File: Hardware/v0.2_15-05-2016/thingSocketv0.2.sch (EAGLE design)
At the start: 32 parts

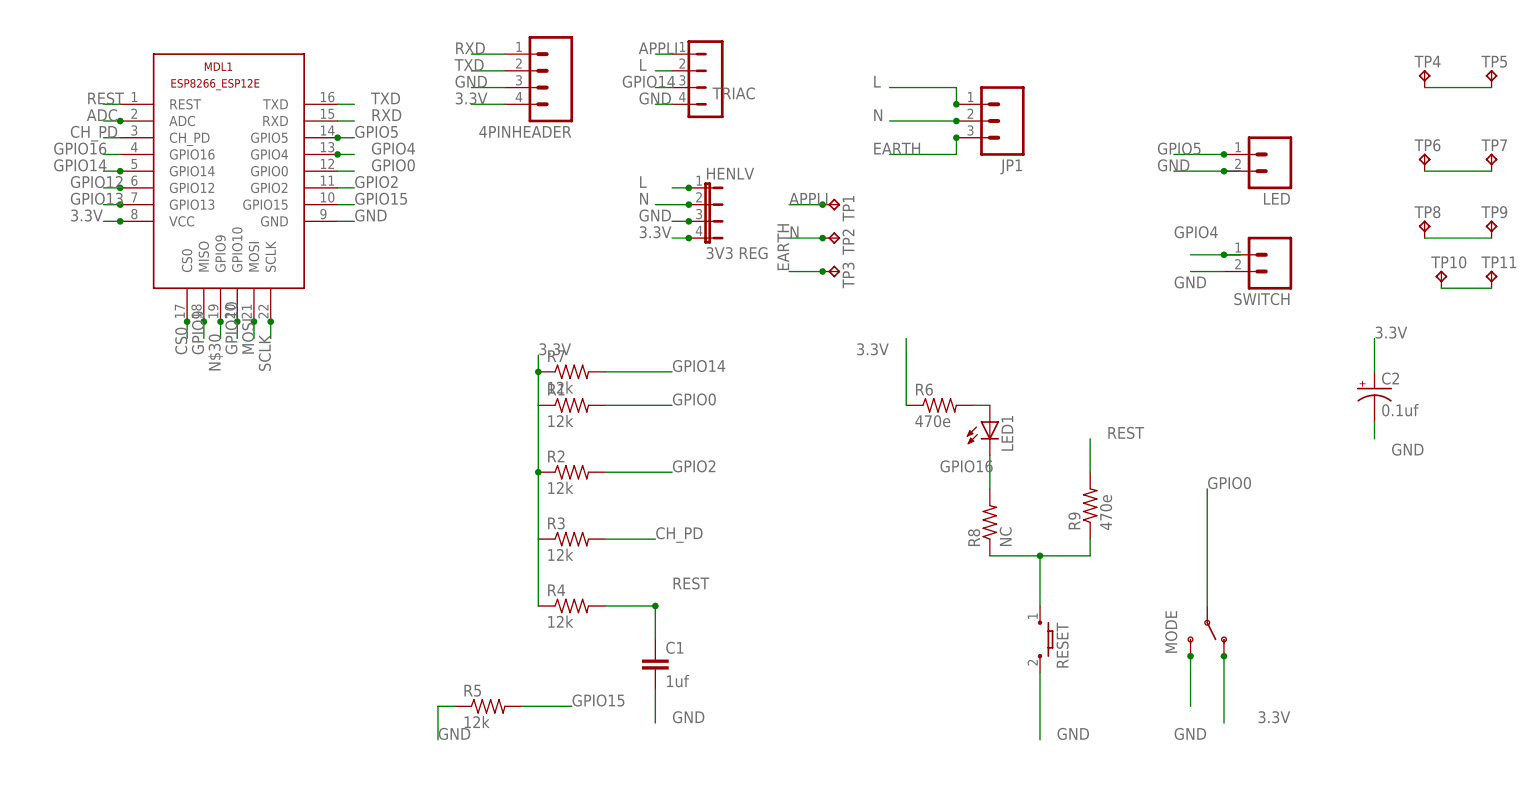
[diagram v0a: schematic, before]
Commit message: unified the resource mechanism; added device password
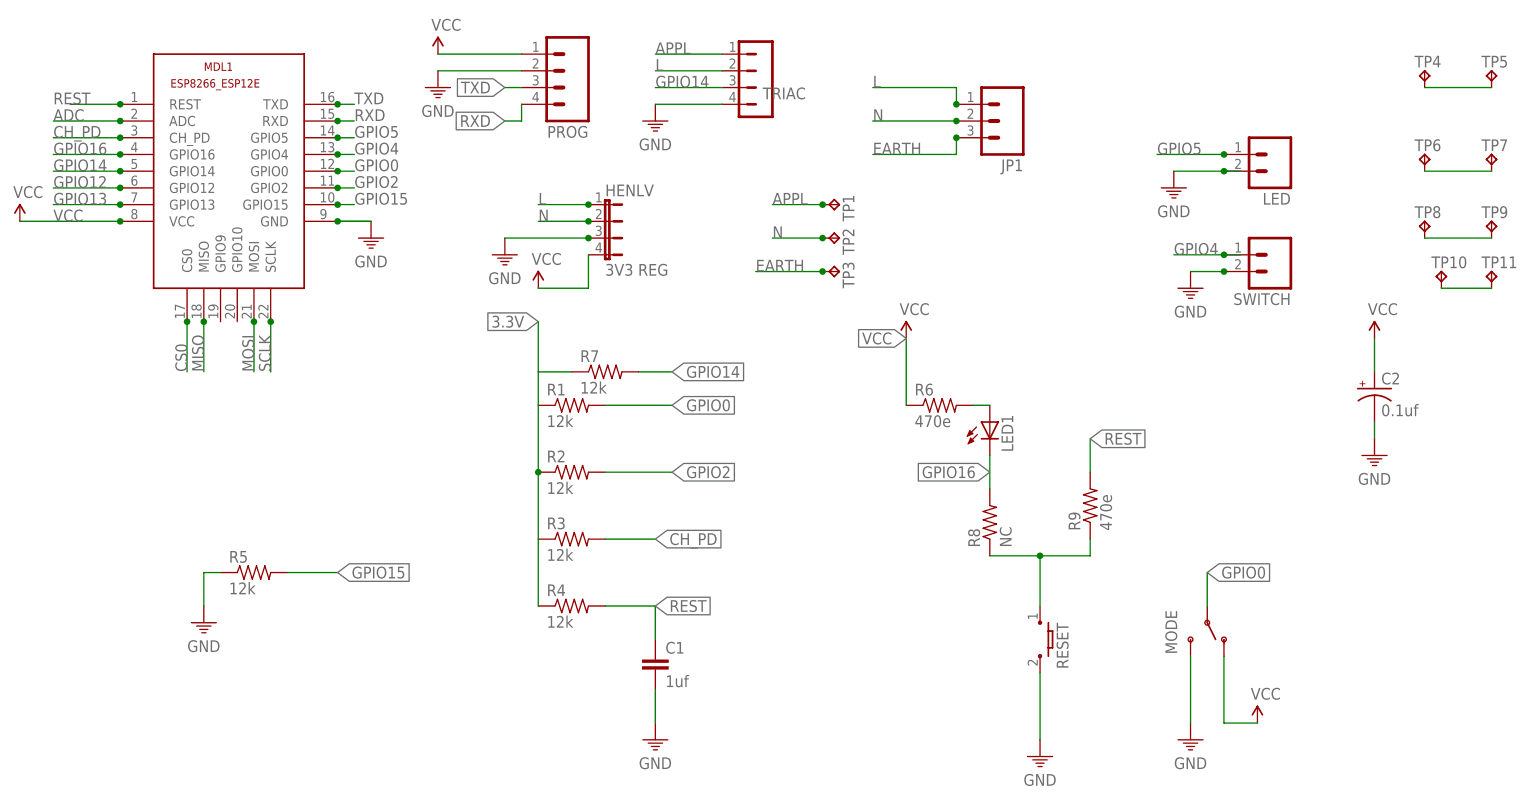
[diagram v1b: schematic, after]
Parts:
- removed 4PINHEADER: (no value), con-oupiin:M04-V
- added PROG: (no value), con-oupiin:M04-V
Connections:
- net APPLI renamed APPL
- net GPIO9 renamed MISO
- removed net GPIO10: MDL1.GPIO10
- removed net N$30: MDL1.GPIO9
- new net VCC: C2.+, HENLV.4, MDL1.VCC, MODE.O, PROG.1, R6.1
- net 3.3V: no longer 4PINHEADER.4, C2.+, HENLV.4, MDL1.VCC, MODE.O, R6.1
- net GND: no longer 4PINHEADER.3
- net RXD: now also PROG.4; no longer 4PINHEADER.1
- net TXD: now also PROG.2, PROG.3; no longer 4PINHEADER.2
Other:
- moved on the sheet: HENLV, R5, R7, TRIAC

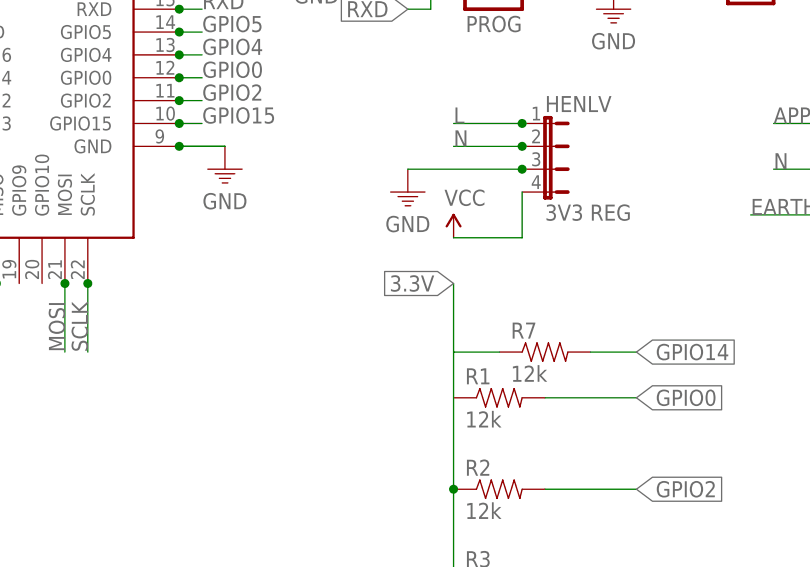
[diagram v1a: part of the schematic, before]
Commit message: added default mechanism for factory reset
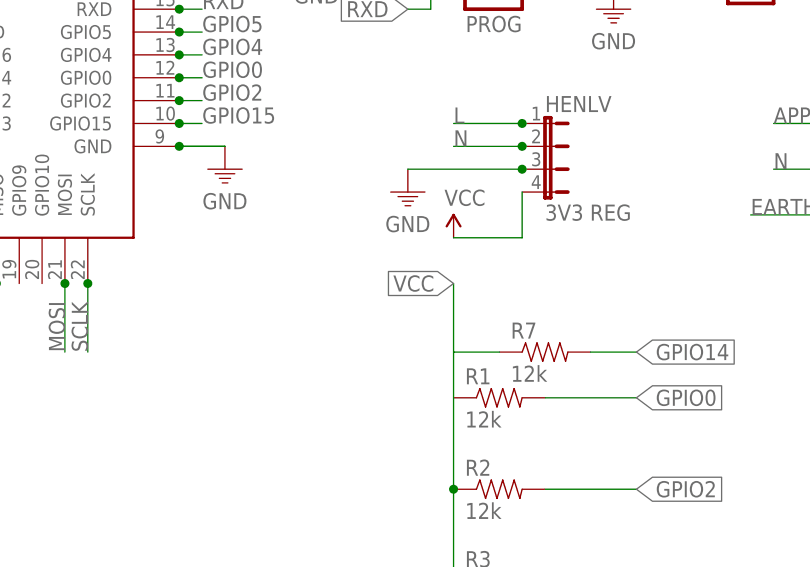
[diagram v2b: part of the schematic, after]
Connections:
- removed net 3.3V: R1.1, R2.1, R3.1, R4.1, R7.1
- net VCC: now also R1.1, R2.1, R3.1, R4.1, R7.1
